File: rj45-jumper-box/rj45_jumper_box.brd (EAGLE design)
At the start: 50 x 25 mm, 4 parts, among them X1 SS-7188S-A-NF, X2 SS-7188S-A-NF

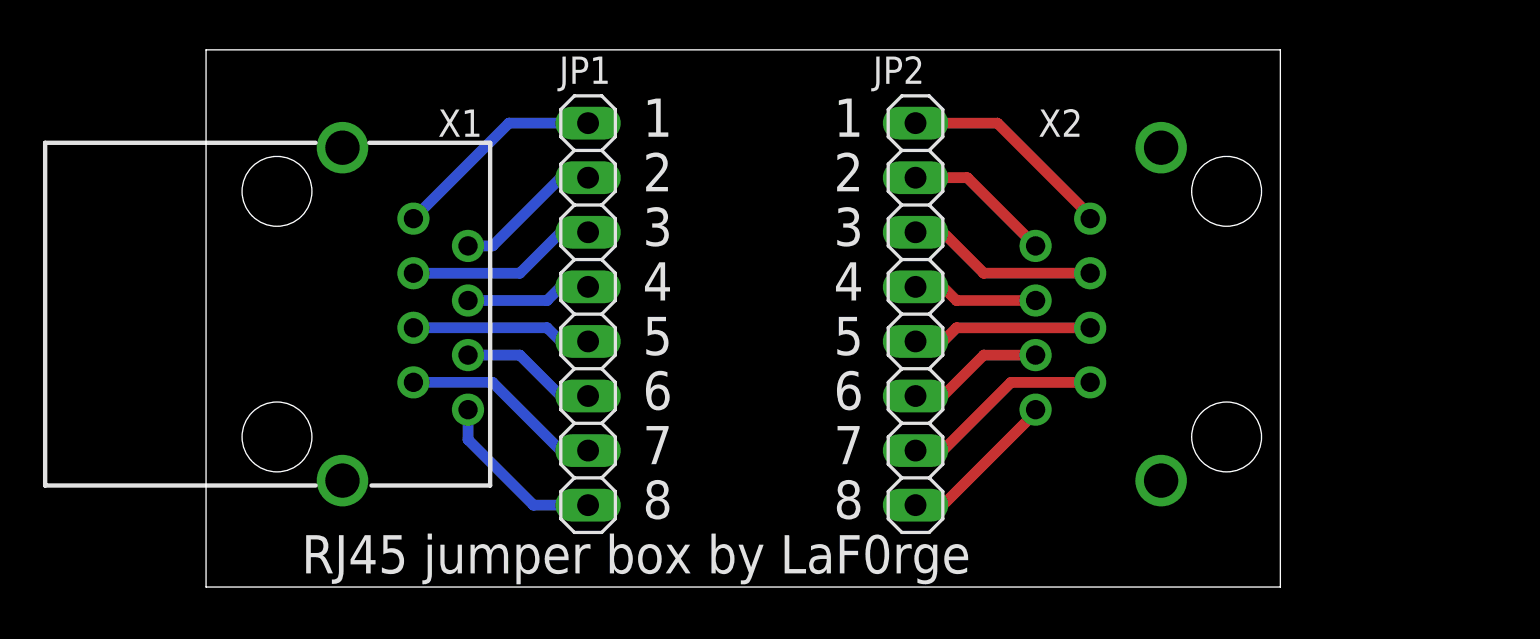
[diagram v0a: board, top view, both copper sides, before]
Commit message: rj45_jumper_box: Use different RJ45 jack; both on top layer
The original design (one RJ45 on top, one on bottom) was easy to route
but was difficult to handle. Let's swap both connectors to top, and use
a low-cost Chinese RJ45.
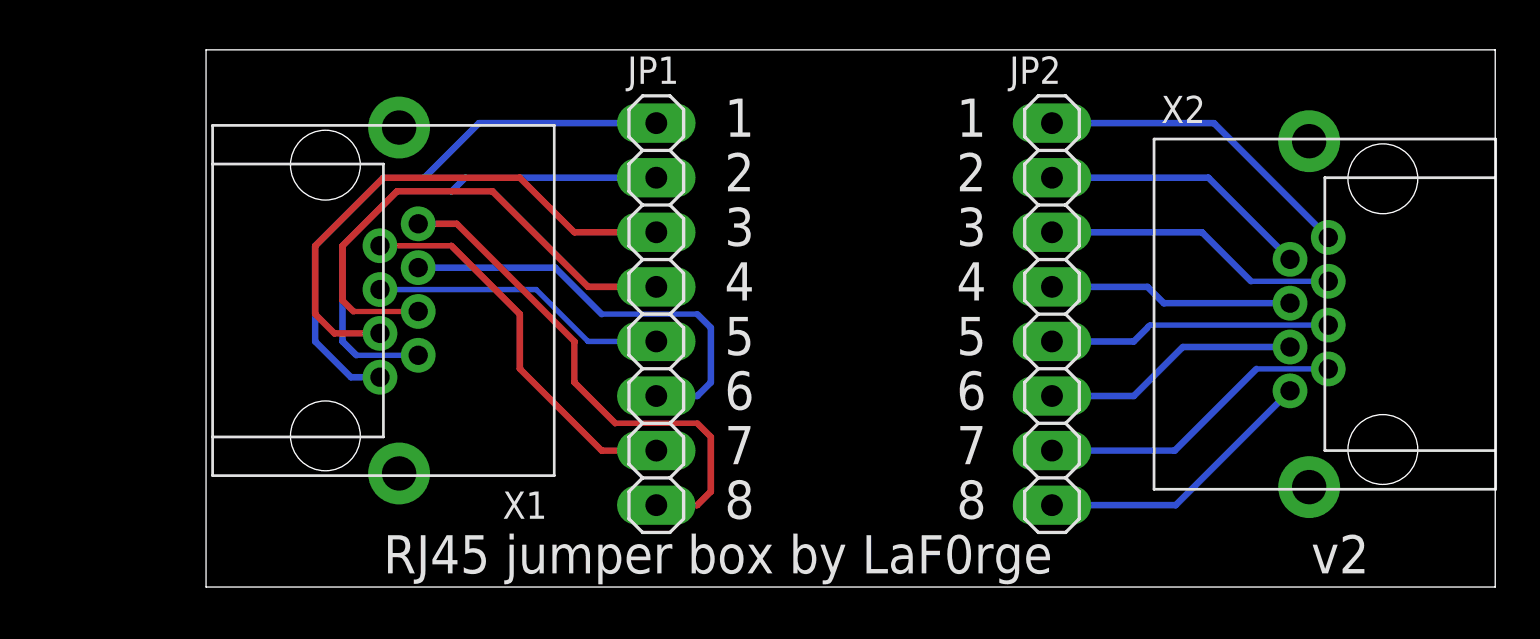
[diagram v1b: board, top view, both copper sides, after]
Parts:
- X1, X2: value SS-7188S-A-NF -> RJ45-RC01133; device stewart-rj45:SS-7188S-A-NF -> stewart-rj45:RC01133
- moved X2 6.35 mm to (52.1, 12.7), flipped to the top
- moved JP2 6.35 mm to (39.4, 12.7)
- moved X1 3.24 mm to (8.26, 13.3), turned to 90 degrees
- moved JP1 3.17 mm to (21.0, 12.7)
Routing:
- net N$4: track 5.85 -> 23.8 mm
- net N$2: track 6.90 -> 24.2 mm
- net X1_1: track 9.97 -> 26.4 mm
- net N$8: track 8.25 -> 24.2 mm
- net N$3: track 8.92 -> 24.8 mm
- net N$6: track 6.38 -> 20.1 mm
- net N$7: track 9.44 -> 18.3 mm
- net N$12: track 5.85 -> 12.0 mm
- net N$5: track 8.39 -> 14.5 mm
- net N$16: track 7.50 -> 13.3 mm
- net N$10: track 6.90 -> 12.7 mm
- net N$14: track 6.38 -> 12.0 mm
- net X2_1: track 10.0 -> 15.1 mm
- net N$15: track 9.44 -> 14.4 mm
- net N$11: track 8.92 -> 13.8 mm
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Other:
- board size 50 x 25 mm -> 60 x 25 mm
- board text added: ">REVISION"
- board text removed: "X2"

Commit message: rj45_jumper_box: Connect shield of two connectors
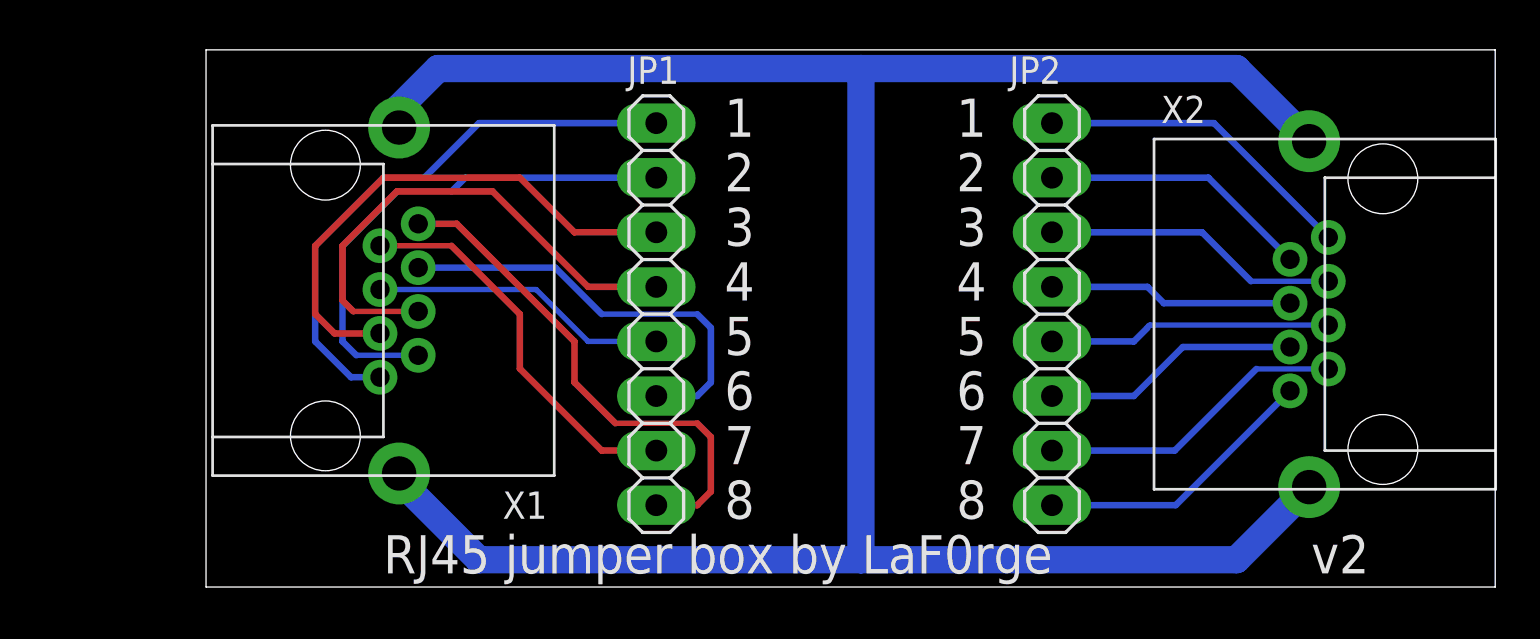
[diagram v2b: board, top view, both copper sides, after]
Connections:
- new net N$1: X1.SHLD1, X1.SHLD2, X2.SHLD1, X2.SHLD2
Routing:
- net N$1: track 0.00 -> 113.9 mm
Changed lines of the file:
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@@
 <wire x1="45.13" y1="3.81" x2="50.45" y2="9.13" width="0.3048" layer="16"/>
+</signal>
+<signal name="N$1">
+<contactref element="X1" pad="SHLD2"/>
+<contactref element="X2" pad="SHLD2"/>
+<contactref element="X2" pad="SHLD1"/>
+<contactref element="X1" pad="SHLD1"/>
+<wire x1="8.985" y1="21.385" x2="8.985" y2="22.32" width="1.27" layer="16"/>
+<wire x1="8.985" y1="22.32" x2="10.795" y2="24.13" width="1.27" layer="16"/>
+<wire x1="10.795" y1="24.13" x2="30.48" y2="24.13" width="1.27" layer="16"/>
+<wire x1="8.985" y1="5.285" x2="8.985" y2="4.985" width="1.27" layer="16"/>
+<wire x1="8.985" y1="4.985" x2="12.7" y2="1.27" width="1.27" layer="16"/>
+<wire x1="12.7" y1="1.27" x2="30.48" y2="1.27" width="1.27" layer="16"/>
+<wire x1="30.48" y1="1.27" x2="47.96" y2="1.27" width="1.27" layer="16"/>
+<wire x1="47.96" y1="1.27" x2="51.34" y2="4.65" width="1.27" layer="16"/>
+<wire x1="51.34" y1="20.75" x2="47.96" y2="24.13" width="1.27" layer="16"/>
+<wire x1="47.96" y1="24.13" x2="30.48" y2="24.13" width="1.27" layer="16"/>
+<wire x1="30.48" y1="24.13" x2="30.48" y2="1.27" width="1.27" layer="16"/>
 </signal>
 </signals>

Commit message: rj45_jumper_box: Add OSWH + sysmocom logo; final v2 as ordered
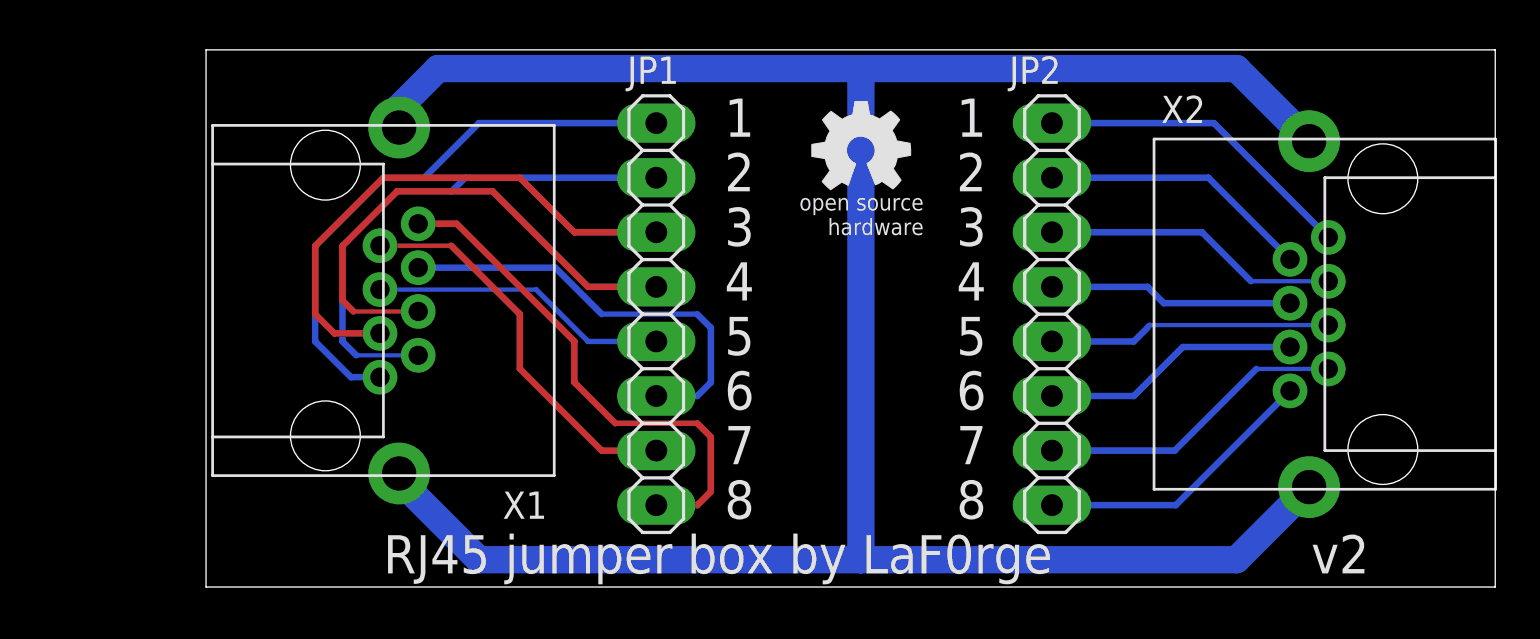
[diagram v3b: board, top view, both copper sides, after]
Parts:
- added U$1: (no value), oshw:OSHW_5MM
- added U$2: (no value), sysmocom-logo:SYSMOCOM-20-BPLACE
- JP1: value (none) -> JP1
- JP2: value (none) -> JP2
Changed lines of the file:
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@@
 <layer number="48" name="Document" color="7" fill="1" visible="yes" active="yes"/>
 <layer number="49" name="Reference" color="7" fill="1" visible="yes" active="yes"/>
+<layer number="50" name="dxf" color="7" fill="1" visible="no" active="no"/>
 <layer number="51" name="tDocu" color="7" fill="1" visible="yes" active="yes"/>
 <layer number="52" name="bDocu" color="7" fill="1" visible="yes" active="yes"/>
+<layer number="53" name="tGND_GNDA" color="7" fill="9" visible="no" active="no"/>
+<layer number="54" name="bGND_GNDA" color="1" fill="9" visible="no" active="no"/>
+<layer number="56" name="wert" color="7" fill="1" visible="no" active="no"/>
 <layer number="90" name="Modules" color="5" fill="1" visible="no" active="no"/>
 <layer number="91" name="Nets" color="2" fill="1" visible="no" active="no"/>
@@
 <layer number="97" name="Info" color="7" fill="1" visible="no" active="no"/>
 <layer number="98" name="Guide" color="6" fill="1" visible="no" active="no"/>
+<layer number="100" name="Muster" color="7" fill="1" visible="no" active="no"/>
+<layer number="101" name="Patch_Top" color="12" fill="4" visible="yes" active="yes"/>
+<layer number="102" name="Vscore" color="7" fill="1" visible="yes" active="yes"/>
+<layer number="103" name="tMap" color="7" fill="1" visible="yes" active="yes"/>
+<layer number="104" name="Name" color="7" fill="1" visible="yes" active="yes"/>
+<layer number="105" name="tPlate" color="7" fill="1" visible="yes" active="yes"/>
+<layer number="106" name="bPlate" color="7" fill="1" visible="yes" active="yes"/>
+<layer number="107" name="Crop" color="7" fill="1" visible="yes" active="yes"/>
+<layer number="116" name="Patch_BOT" color="9" fill="4" visible="yes" active="yes"/>
+<layer number="121" name="_tsilk" color="7" fill="1" visible="yes" active="yes"/>
+<layer number="122" name="_bsilk" color="7" fill="1" visible="yes" active="yes"/>
+<layer number="125" name="_tNames" color="7" fill="1" visible="yes" active="yes"/>
+<layer number="144" name="Drill_legend" color="7" fill="1" visible="yes" active="yes"/>
+<layer number="151" name="HeatSink" color="7" fill="1" visible="yes" active="yes"/>
+<layer number="200" name="200bmp" color="1" fill="10" visible="yes" active="yes"/>
+<layer number="201" name="201bmp" color="2" fill="1" visible="no" active="no"/>
+<layer number="202" name="202bmp" color="3" fill="1" visible="no" active="no"/>
+<layer number="203" name="203bmp" color="4" fill="10" visible="yes" active="yes"/>
+<layer number="204" name="204bmp" color="5" fill="10" visible="yes" active="yes"/>
+<layer number="205" name="205bmp" color="6" fill="10" visible="yes" active="yes"/>
+<layer number="206" name="206bmp" color="7" fill="10" visible="yes" active="yes"/>
+<layer number="207" name="207bmp" color="8" fill="10" visible="yes" active="yes"/>
+<layer number="208" name="208bmp" color="9" fill="10" visible="yes" active="yes"/>
+<layer number="209" name="209bmp" color="7" fill="1" visible="yes" active="yes"/>
+<layer number="210" name="210bmp" color="7" fill="1" visible="yes" active="yes"/>
+<layer number="211" name="211bmp" color="7" fill="1" visible="yes" active="yes"/>
+<layer number="212" name="212bmp" color="7" fill="1" visible="yes" active="yes"/>
+<layer number="213" name="213bmp" color="7" fill="1" visible="yes" active="yes"/>
+<layer number="214" name="214bmp" color="7" fill="1" visible="yes" active="yes"/>
+<layer number="215" name="215bmp" color="7" fill="1" visible="yes" active="yes"/>
+<layer number="216" name="216bmp" color="7" fill="1" visible="yes" active="yes"/>
+<layer number="250" name="Descript" color="3" fill="1" visible="no" active="no"/>
+<layer number="251" name="SMDround" color="12" fill="11" visible="no" active="no"/>
+<layer number="254" name="cooling" color="7" fill="1" visible="yes" active="yes"/>
 </layers>
 <board>
@@
 </autorouter>
 <elements>
-<element name="JP1" library="pinhead" package="1X08" value="" x="20.955" y="12.7" smashed="yes" rot="R270">
+<element name="JP1" library="pinhead" package="1X08" value="JP1" x="20.955" y="12.7" smashed="yes" rot="R270">
 <attribute name="NAME" x="19.6088" y="23.4188" size="1.27" layer="25" font="vector" ratio="14"/>
 <attribute name="VALUE" x="17.78" y="22.86" size="1.27" layer="27" rot="R270"/>
+<attribute name="LCSC_PART" value="C706880" x="20.955" y="12.7" size="1.778" layer="27" font="vector" ratio="14" rot="R270" display="off"/>
 </element>
-<element name="JP2" library="pinhead" package="1X08" value="" x="39.37" y="12.7" smashed="yes" rot="R270">
+<element name="JP2" library="pinhead" package="1X08" value="JP2" x="39.37" y="12.7" smashed="yes" rot="R270">
 <attribute name="NAME" x="37.3888" y="23.4188" size="1.27" layer="25" font="vector" ratio="14"/>
 <attribute name="VALUE" x="36.195" y="22.86" size="1.27" layer="27" rot="R270"/>
+<attribute name="LCSC_PART" value="C706880" x="39.37" y="12.7" size="1.778" layer="27" font="vector" ratio="14" rot="R270" display="off"/>
 </element>
-<element name="X1" library="stewart-rj45" package="RC01133" value="RJ45-RC01133" x="8.255" y="13.335" rot="R90"/>
-<element name="X2" library="stewart-rj45" package="RC01133" value="RJ45-RC01133" x="52.07" y="12.7" rot="R270"/>
+<element name="X1" library="stewart-rj45" package="RC01133" value="RJ45-RC01133" x="8.255" y="13.335" rot="R90">
+<attribute name="LCSC_PART" value="C708616" x="8.255" y="13.335" size="1.778" layer="27" font="vector" ratio="14" rot="R90" display="off"/>
+</element>
+<element name="X2" library="stewart-rj45" package="RC01133" value="RJ45-RC01133" x="52.07" y="12.7" rot="R270">
+<attribute name="LCSC_PART" value="C708616" x="52.07" y="12.7" size="1.778" layer="27" font="vector" ratio="14" rot="R270" display="off"/>
+</element>
+<element name="U$1" library="oshw" package="OSHW_5MM" value="" x="30.48" y="20.32"/>
+<element name="U$2" library="sysmocom-logo" package="SYSMOCOM-20-BPLACE" value="" x="29.21" y="2.54" rot="R90"/>
 </elements>
 <signals>
@@
 <contactref element="X1" pad="2"/>
 <contactref element="JP1" pad="2"/>
-<wire x1="9.875" y1="10.785" x2="6.995" y2="10.785" width="0.25" layer="16"/>
+<wire x1="9.875" y1="10.785" x2="6.995" y2="10.785" width="0.2" layer="16"/>
 <wire x1="6.995" y1="10.785" x2="6.35" y2="11.43" width="0.3048" layer="16"/>
 <wire x1="6.35" y1="11.43" x2="6.35" y2="15.875" width="0.3048" layer="16"/>
@@
 <contactref element="X1" pad="4"/>
 <contactref element="JP1" pad="4"/>
-<wire x1="9.875" y1="12.825" x2="6.86" y2="12.825" width="0.25" layer="1"/>
+<wire x1="9.875" y1="12.825" x2="6.86" y2="12.825" width="0.2" layer="1"/>
 <wire x1="6.86" y1="12.825" x2="6.35" y2="13.335" width="0.3048" layer="1"/>
 <wire x1="6.35" y1="13.335" x2="6.35" y2="15.875" width="0.3048" layer="1"/>
@@
 <contactref element="X1" pad="5"/>
 <contactref element="JP1" pad="5"/>
-<wire x1="8.095" y1="13.845" x2="15.365" y2="13.845" width="0.25" layer="16"/>
+<wire x1="8.095" y1="13.845" x2="15.365" y2="13.845" width="0.2" layer="16"/>
 <wire x1="15.365" y1="13.845" x2="17.78" y2="11.43" width="0.25" layer="16"/>
 <wire x1="17.78" y1="11.43" x2="20.955" y2="11.43" width="0.25" layer="16"/>
@@
 <contactref element="X1" pad="7"/>
 <contactref element="JP1" pad="7"/>
-<wire x1="8.095" y1="15.885" x2="11.42" y2="15.885" width="0.25" layer="1"/>
+<wire x1="8.095" y1="15.885" x2="11.42" y2="15.885" width="0.2" layer="1"/>
 <wire x1="11.42" y1="15.885" x2="14.605" y2="12.7" width="0.3048" layer="1"/>
 <wire x1="14.605" y1="12.7" x2="14.605" y2="10.16" width="0.3048" layer="1"/>
@@
 <contactref element="JP2" pad="3"/>
 <contactref element="X2" pad="3"/>
-<wire x1="52.23" y1="14.23" x2="48.635" y2="14.23" width="0.25" layer="16"/>
+<wire x1="52.23" y1="14.23" x2="48.635" y2="14.23" width="0.2" layer="16"/>
 <wire x1="48.635" y1="14.23" x2="46.355" y2="16.51" width="0.3048" layer="16"/>
 <wire x1="46.355" y1="16.51" x2="39.37" y2="16.51" width="0.3048" layer="16"/>
@@
 <contactref element="JP2" pad="5"/>
 <contactref element="X2" pad="5"/>
-<wire x1="52.23" y1="12.19" x2="43.94" y2="12.19" width="0.25" layer="16"/>
+<wire x1="52.23" y1="12.19" x2="43.94" y2="12.19" width="0.2" layer="16"/>
 <wire x1="43.94" y1="12.19" x2="43.815" y2="12.065" width="0.25" layer="16" curve="90"/>
 <wire x1="43.815" y1="12.065" x2="43.18" y2="11.43" width="0.3048" layer="16"/>
@@
 <contactref element="JP2" pad="7"/>
 <contactref element="X2" pad="7"/>
-<wire x1="52.23" y1="10.15" x2="48.885" y2="10.15" width="0.25" layer="16"/>
+<wire x1="52.23" y1="10.15" x2="48.885" y2="10.15" width="0.2" layer="16"/>
 <wire x1="48.885" y1="10.15" x2="45.085" y2="6.35" width="0.3048" layer="16"/>
 <wire x1="45.085" y1="6.35" x2="39.37" y2="6.35" width="0.3048" layer="16"/>
@@
 </board>
 </drawing>
+<compatibility>
+<note version="6.3" minversion="6.2.2" severity="warning">
+Since Version 6.2.2 text objects can contain more than one line,
+which will not be processed correctly with this version.
+</note>
+</compatibility>
 </eagle>
